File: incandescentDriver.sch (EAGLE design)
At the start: 36 parts, among them IC2 7805, IC5 74LS595N, J1 HEADER, J10 HEADER, J11 POWER_JACKPTH_LOCK, J2 HEADER, J3 HEADER, J4 HEADER, J5 HEADER, J6 HEADER, J7 HEADER, J8 HEADER, J9 HEADER

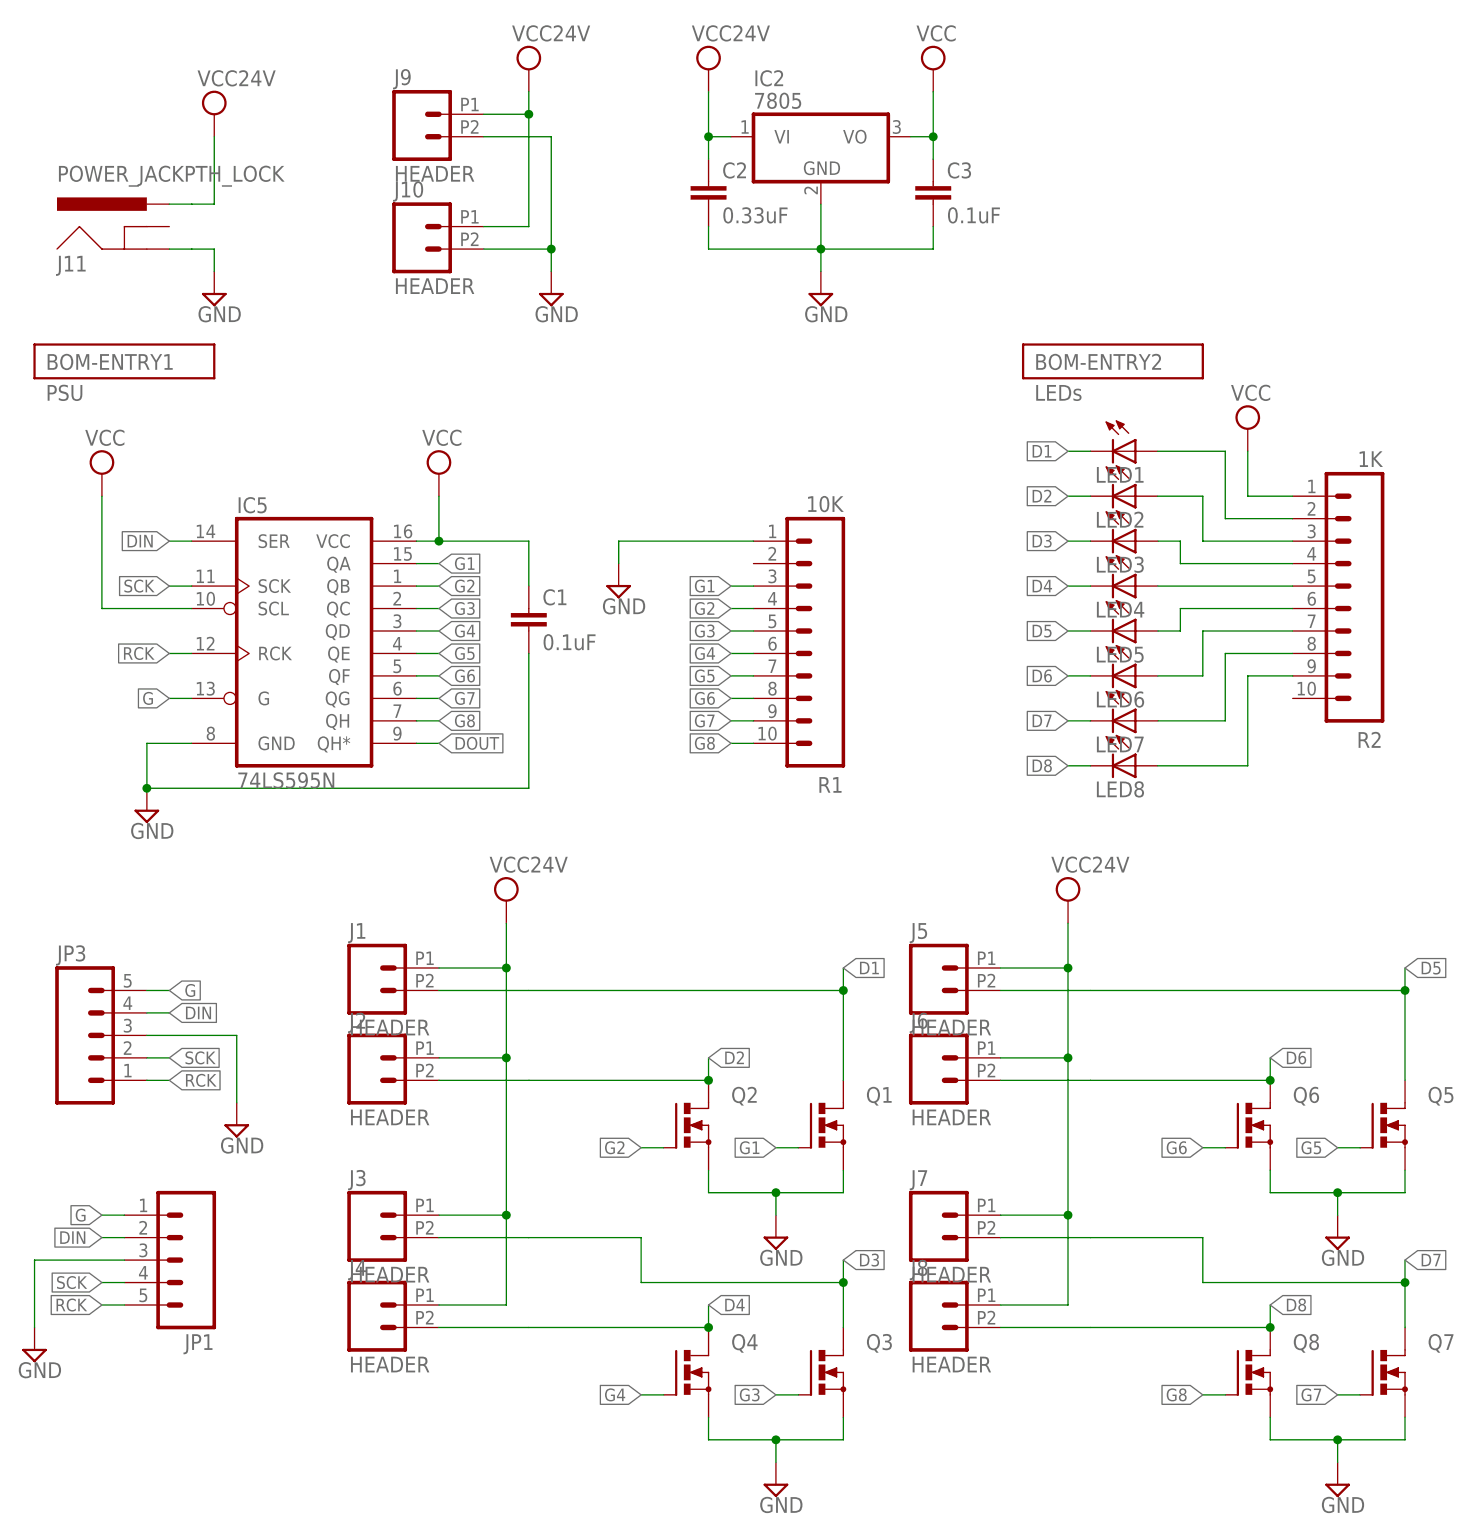
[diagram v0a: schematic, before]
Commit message: updated incandescent driver to 1.0
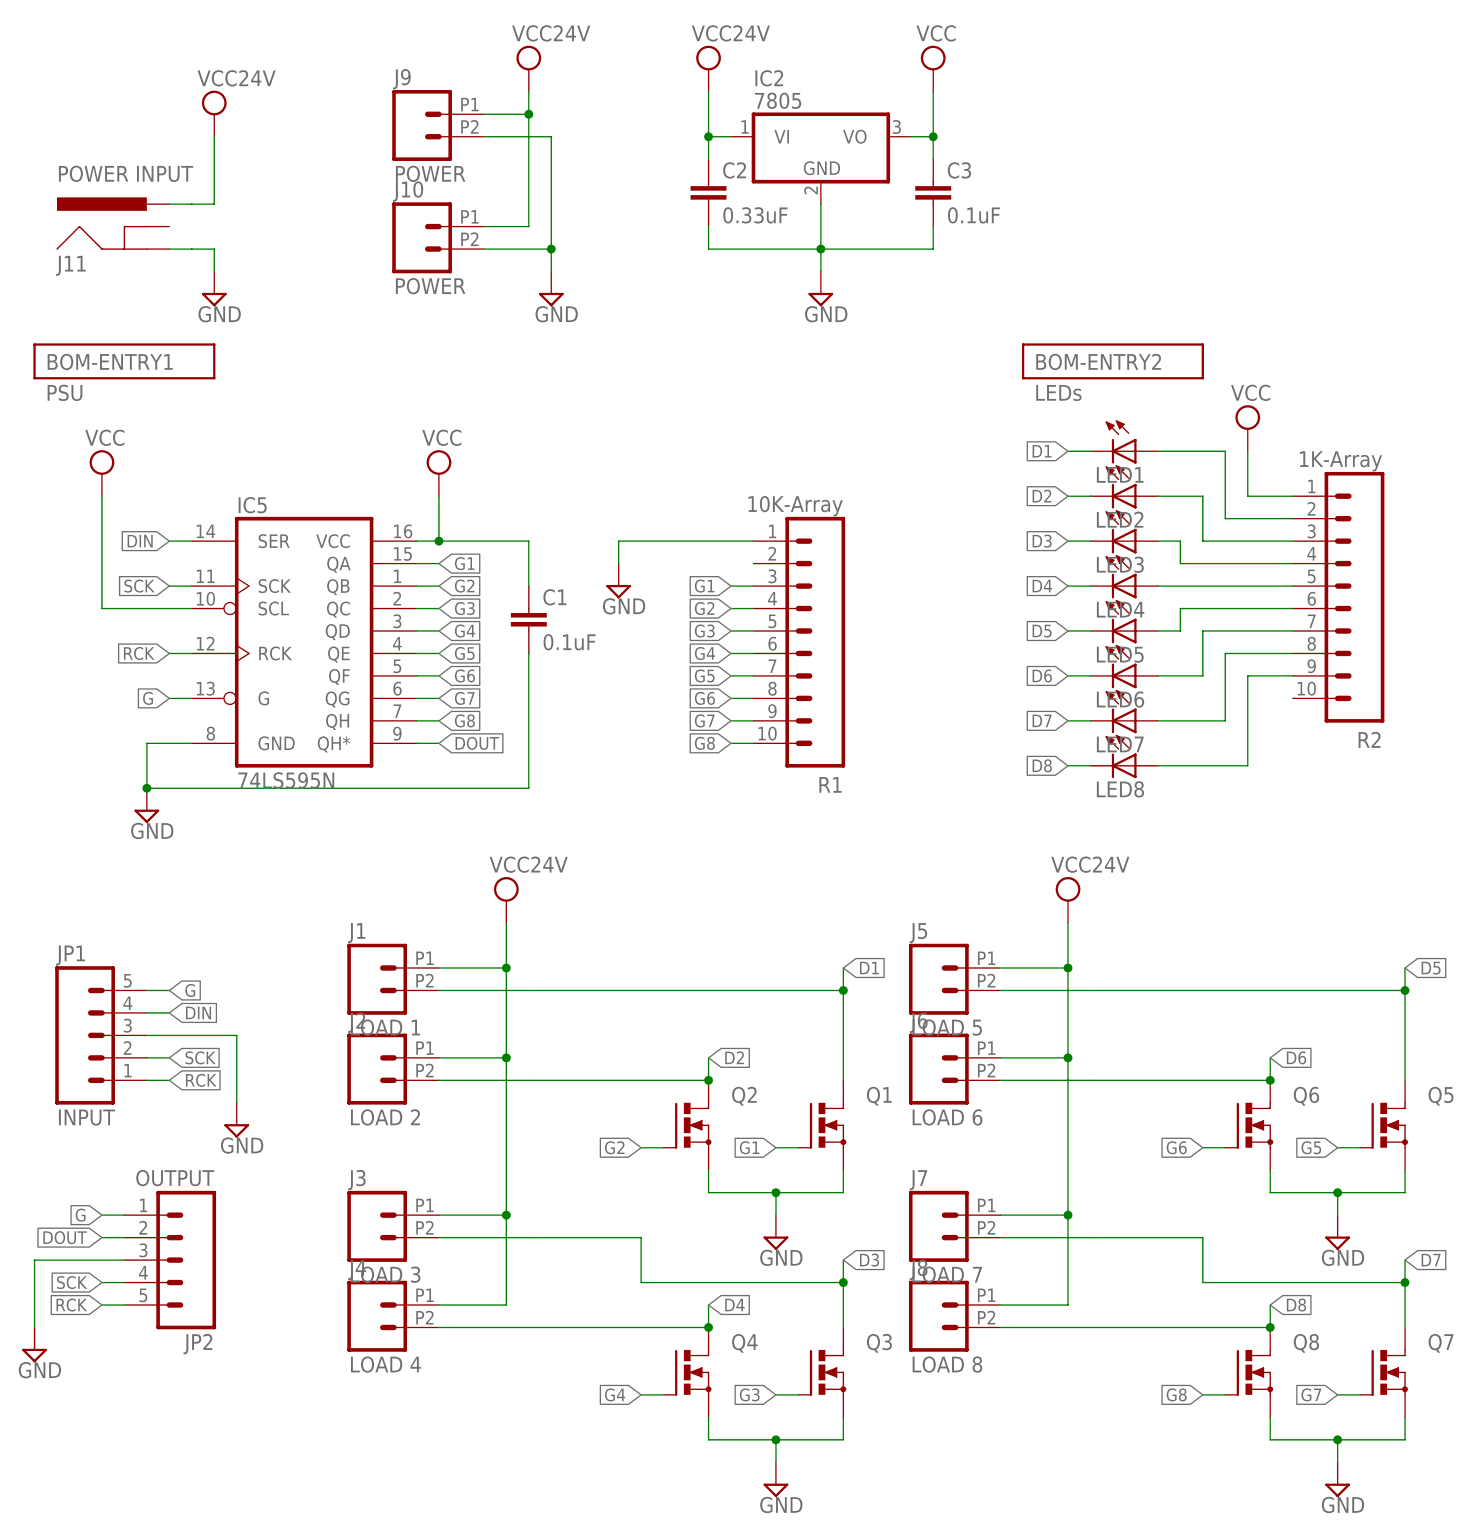
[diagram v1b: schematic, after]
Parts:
- removed JP3: (no value), SparkFun-Connectors:M05LOCK
- added JP2: OUTPUT, SparkFun-Connectors:M05LOCK
- J1: value HEADER -> LOAD 1
- J10, J9: value HEADER -> POWER
- J11: value POWER_JACKPTH_LOCK -> POWER INPUT
- J2: value HEADER -> LOAD 2
- J3: value HEADER -> LOAD 3
- J4: value HEADER -> LOAD 4
- J5: value HEADER -> LOAD 5
- J6: value HEADER -> LOAD 6
- J7: value HEADER -> LOAD 7
- J8: value HEADER -> LOAD 8
- JP1: value (none) -> INPUT
- R1: value 10K -> 10K-Array
- R2: value 1K -> 1K-Array
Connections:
- net DIN: now also JP1.4; no longer JP1.2, JP3.4
- net DOUT: now also JP2.2
- net G: now also JP1.5, JP2.1; no longer JP1.1, JP3.5
- net GND: now also JP2.3; no longer JP3.3
- net RCK: now also JP1.1, JP2.5; no longer JP1.5, JP3.1
- net SCK: now also JP1.2, JP2.4; no longer JP1.4, JP3.2
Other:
- moved on the sheet: JP1
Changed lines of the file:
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@@
 </classes>
 <parts>
-<part name="J1" library="Livestream" deviceset="HEADER" device="">
-<attribute name="PARTNO" value="OSTTC022162"/>
-</part>
-<part name="J2" library="Livestream" deviceset="HEADER" device="">
-<attribute name="PARTNO" value="OSTTC022162"/>
-</part>
-<part name="J3" library="Livestream" deviceset="HEADER" device="">
-<attribute name="PARTNO" value="OSTTC022162"/>
-</part>
-<part name="J4" library="Livestream" deviceset="HEADER" device="">
+<part name="J1" library="Livestream" deviceset="HEADER" device="" value="LOAD 1">
+<attribute name="PARTNO" value="OSTTC022162"/>
+</part>
+<part name="J2" library="Livestream" deviceset="HEADER" device="" value="LOAD 2">
+<attribute name="PARTNO" value="OSTTC022162"/>
+</part>
+<part name="J3" library="Livestream" deviceset="HEADER" device="" value="LOAD 3">
+<attribute name="PARTNO" value="OSTTC022162"/>
+</part>
+<part name="J4" library="Livestream" deviceset="HEADER" device="" value="LOAD 4">
 <attribute name="PARTNO" value="OSTTC022162"/>
 </part>
@@
 <attribute name="PARTNO" value="SR295E104MAR"/>
 </part>
-<part name="JP3" library="SparkFun-Connectors" deviceset="M05" device="LOCK">
+<part name="JP1" library="SparkFun-Connectors" deviceset="M05" device="LOCK" value="INPUT">
 <attribute name="PARTNO" value="M20-9960545"/>
 </part>
-<part name="JP1" library="SparkFun-Connectors" deviceset="M05" device="LOCK">
+<part name="JP2" library="SparkFun-Connectors" deviceset="M05" device="LOCK" value="OUTPUT">
 <attribute name="PARTNO" value="M20-9960545"/>
 </part>
 <part name="SUPPLY6" library="supply2" deviceset="GND" device=""/>
-<part name="J11" library="SparkFun-Connectors" deviceset="POWER_JACK" device="PTH_LOCK">
+<part name="J11" library="SparkFun-Connectors" deviceset="POWER_JACK" device="PTH_LOCK" value="POWER INPUT">
 <attribute name="PARTNO" value="PJ-202A"/>
 </part>
 <part name="\VAL3" library="supply2" deviceset="VCC" device="" value="VCC24V"/>
 <part name="SUPPLY2" library="supply2" deviceset="GND" device=""/>
-<part name="J9" library="Livestream" deviceset="HEADER" device="">
+<part name="J9" library="Livestream" deviceset="HEADER" device="" value="POWER">
 <attribute name="DNP" value="T"/>
 <attribute name="PARTNO" value="OSTTC022162"/>
 </part>
-<part name="J10" library="Livestream" deviceset="HEADER" device="">
+<part name="J10" library="Livestream" deviceset="HEADER" device="" value="POWER">
 <attribute name="DNP" value="T"/>
 <attribute name="PARTNO" value="OSTTC022162"/>
@@
 <part name="\VAL4" library="supply2" deviceset="VCC" device="" value="VCC24V"/>
 <part name="SUPPLY7" library="supply2" deviceset="GND" device=""/>
-<part name="R1" library="SparkFun-Connectors" deviceset="M10" device="LOCK" value="10K">
+<part name="R1" library="SparkFun-Connectors" deviceset="M10" device="LOCK" value="10K-Array">
 <attribute name="PARTNO" value="L101S103LF"/>
 </part>
@@
 <part name="SUPPLY8" library="supply2" deviceset="GND" device=""/>
 <part name="SUPPLY1" library="supply2" deviceset="GND" device=""/>
-<part name="J5" library="Livestream" deviceset="HEADER" device="">
-<attribute name="PARTNO" value="OSTTC022162"/>
-</part>
-<part name="J6" library="Livestream" deviceset="HEADER" device="">
-<attribute name="PARTNO" value="OSTTC022162"/>
-</part>
-<part name="J7" library="Livestream" deviceset="HEADER" device="">
-<attribute name="PARTNO" value="OSTTC022162"/>
-</part>
-<part name="J8" library="Livestream" deviceset="HEADER" device="">
+<part name="J5" library="Livestream" deviceset="HEADER" device="" value="LOAD 5">
+<attribute name="PARTNO" value="OSTTC022162"/>
+</part>
+<part name="J6" library="Livestream" deviceset="HEADER" device="" value="LOAD 6">
+<attribute name="PARTNO" value="OSTTC022162"/>
+</part>
+<part name="J7" library="Livestream" deviceset="HEADER" device="" value="LOAD 7">
+<attribute name="PARTNO" value="OSTTC022162"/>
+</part>
+<part name="J8" library="Livestream" deviceset="HEADER" device="" value="LOAD 8">
 <attribute name="PARTNO" value="OSTTC022162"/>
 </part>
@@
 <part name="SUPPLY9" library="supply2" deviceset="GND" device=""/>
 <part name="SUPPLY10" library="supply2" deviceset="GND" device=""/>
-<part name="R2" library="SparkFun-Connectors" deviceset="M10" device="LOCK" value="1K">
+<part name="R2" library="SparkFun-Connectors" deviceset="M10" device="LOCK" value="1K-Array">
 <attribute name="PARTNO" value="4609X-101-102LF"/>
 </part>
@@
 <attribute name="PARTNO" x="-10.16" y="165.1" size="1.778" layer="96" display="off"/>
 </instance>
-<instance part="JP3" gate="G$1" x="-60.96" y="119.38">
+<instance part="JP1" gate="G$1" x="-60.96" y="119.38">
 <attribute name="PARTNO" x="-60.96" y="119.38" size="1.778" layer="96" display="off"/>
 </instance>
-<instance part="JP1" gate="G$1" x="-48.26" y="93.98" rot="R180">
+<instance part="JP2" gate="G$1" x="-48.26" y="93.98" rot="R180">
 <attribute name="PARTNO" x="-48.26" y="93.98" size="1.778" layer="96" display="off"/>
 </instance>
@@
 </segment>
 <segment>
-<pinref part="JP3" gate="G$1" pin="3"/>
+<pinref part="JP1" gate="G$1" pin="3"/>
 <pinref part="SUPPLY5" gate="GND" pin="GND"/>
 <wire x1="-53.34" y1="119.38" x2="-43.18" y2="119.38" width="0.1524" layer="91"/>
@@
 </segment>
 <segment>
-<pinref part="JP1" gate="G$1" pin="3"/>
+<pinref part="JP2" gate="G$1" pin="3"/>
 <pinref part="SUPPLY6" gate="GND" pin="GND"/>
 <wire x1="-55.88" y1="93.98" x2="-66.04" y2="93.98" width="0.1524" layer="91"/>
@@
 <label x="-20.32" y="152.4" size="1.4224" layer="95" xref="yes"/>
 </segment>
+<segment>
+<pinref part="JP2" gate="G$1" pin="2"/>
+<wire x1="-55.88" y1="96.52" x2="-58.42" y2="96.52" width="0.1524" layer="91"/>
+<label x="-58.42" y="96.52" size="1.4224" layer="95" rot="R180" xref="yes"/>
+</segment>
 </net>
 <net name="G" class="0">
@@
 </segment>
 <segment>
-<pinref part="JP3" gate="G$1" pin="5"/>
+<pinref part="JP1" gate="G$1" pin="5"/>
 <wire x1="-53.34" y1="124.46" x2="-50.8" y2="124.46" width="0.1524" layer="91"/>
 <label x="-50.8" y="124.46" size="1.4224" layer="95" xref="yes"/>
 </segment>
 <segment>
-<pinref part="JP1" gate="G$1" pin="1"/>
+<pinref part="JP2" gate="G$1" pin="1"/>
 <wire x1="-55.88" y1="99.06" x2="-58.42" y2="99.06" width="0.1524" layer="91"/>
 <label x="-58.42" y="99.06" size="1.4224" layer="95" rot="R180" xref="yes"/>
@@
 </segment>
 <segment>
-<pinref part="JP3" gate="G$1" pin="1"/>
+<pinref part="JP1" gate="G$1" pin="1"/>
 <wire x1="-53.34" y1="114.3" x2="-50.8" y2="114.3" width="0.1524" layer="91"/>
 <label x="-50.8" y="114.3" size="1.4224" layer="95" xref="yes"/>
 </segment>
 <segment>
-<pinref part="JP1" gate="G$1" pin="5"/>
+<pinref part="JP2" gate="G$1" pin="5"/>
 <wire x1="-55.88" y1="88.9" x2="-58.42" y2="88.9" width="0.1524" layer="91"/>
 <label x="-58.42" y="88.9" size="1.4224" layer="95" rot="R180" xref="yes"/>
@@
 </segment>
 <segment>
-<pinref part="JP3" gate="G$1" pin="2"/>
+<pinref part="JP1" gate="G$1" pin="2"/>
 <wire x1="-53.34" y1="116.84" x2="-50.8" y2="116.84" width="0.1524" layer="91"/>
 <label x="-50.8" y="116.84" size="1.4224" layer="95" xref="yes"/>
 </segment>
 <segment>
-<pinref part="JP1" gate="G$1" pin="4"/>
+<pinref part="JP2" gate="G$1" pin="4"/>
 <wire x1="-55.88" y1="91.44" x2="-58.42" y2="91.44" width="0.1524" layer="91"/>
 <label x="-58.42" y="91.44" size="1.4224" layer="95" rot="R180" xref="yes"/>
@@
 </segment>
 <segment>
-<pinref part="JP3" gate="G$1" pin="4"/>
+<pinref part="JP1" gate="G$1" pin="4"/>
 <wire x1="-53.34" y1="121.92" x2="-50.8" y2="121.92" width="0.1524" layer="91"/>
 <label x="-50.8" y="121.92" size="1.4224" layer="95" xref="yes"/>
 </segment>
-<segment>
-<pinref part="JP1" gate="G$1" pin="2"/>
-<wire x1="-55.88" y1="96.52" x2="-58.42" y2="96.52" width="0.1524" layer="91"/>
-<label x="-58.42" y="96.52" size="1.4224" layer="95" rot="R180" xref="yes"/>
-</segment>
-</net>
+</net>
